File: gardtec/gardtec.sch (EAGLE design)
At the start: 9 parts, among them IC1 ATMEGA328P

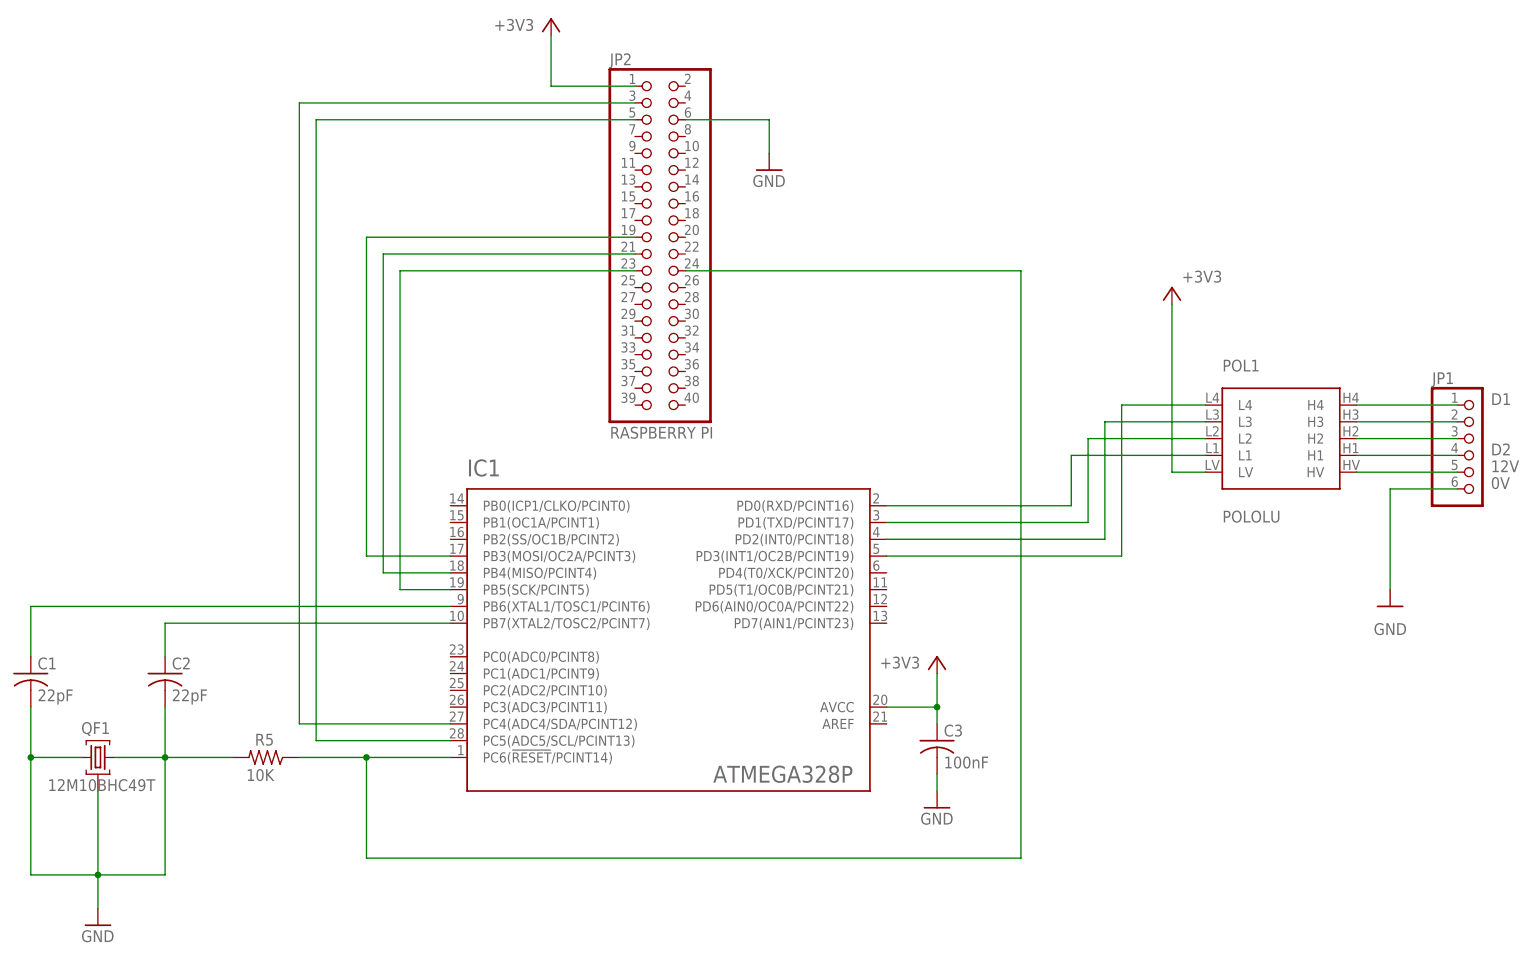
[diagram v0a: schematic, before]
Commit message: fixed wrong reset and xtal connections in schematic
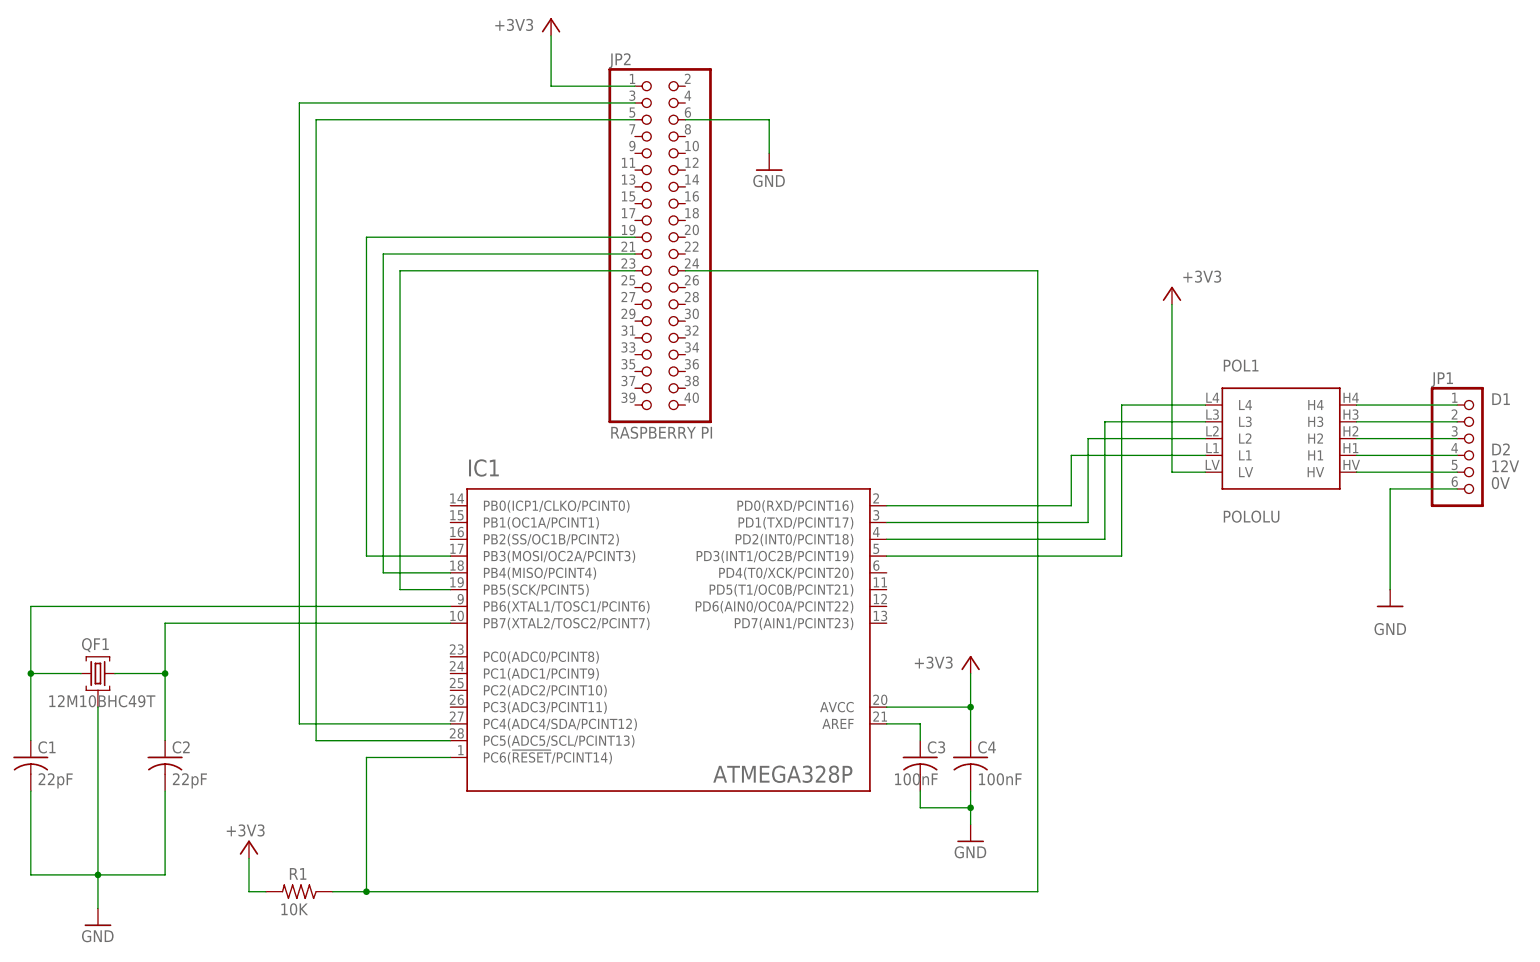
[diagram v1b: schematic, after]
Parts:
- removed R5: 10K, rcl:R-US_R0805
- added C4: 100nF, rcl:C-USC0805
- added R1: 10K, rcl:R-US_R0805
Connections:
- new net N$5: C3.1, IC1IC.AREF
- net +3V3: now also C4.1, R1.2; no longer C3.1
- net 0V: now also C4.2; no longer QF1.1, QF1.3, R5.2
- net N$7: now also QF1.1
- net N$8: now also QF1.3
- net N$9: now also R1.1; no longer R5.1
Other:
- moved on the sheet: C1, C2, C3, QF1
